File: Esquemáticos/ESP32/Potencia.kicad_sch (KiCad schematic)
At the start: 16 parts, among them U1 LM2596S-5

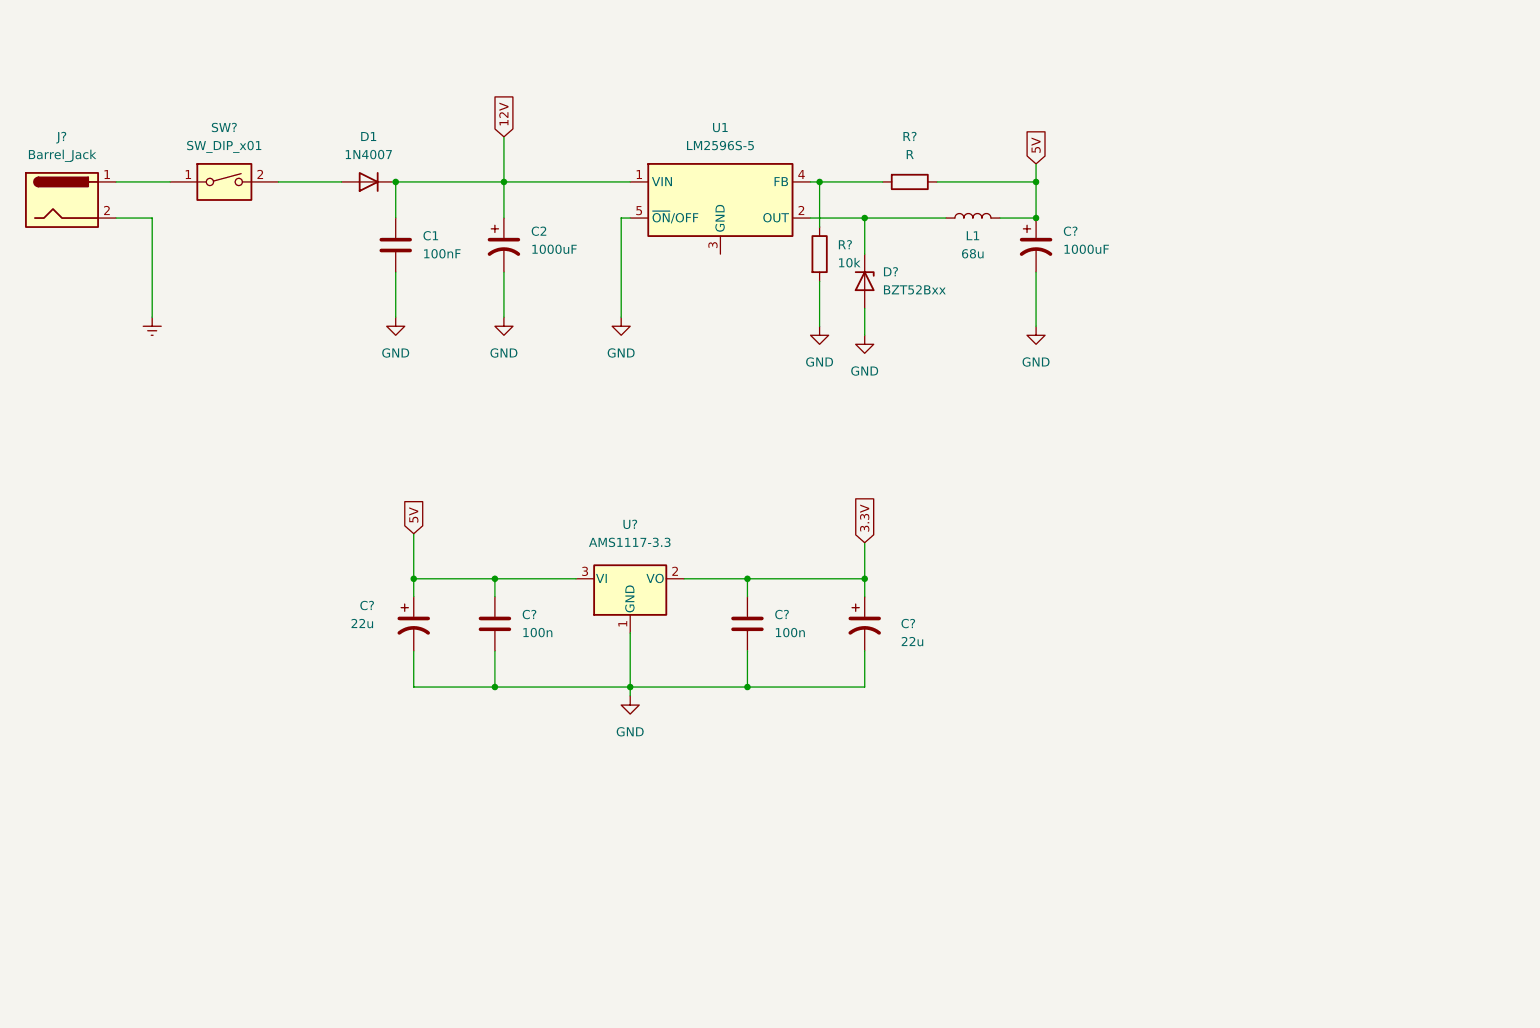
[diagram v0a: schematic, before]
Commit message: Agregada la parte de motores a la jerarquía de esquemáticos
:+1:
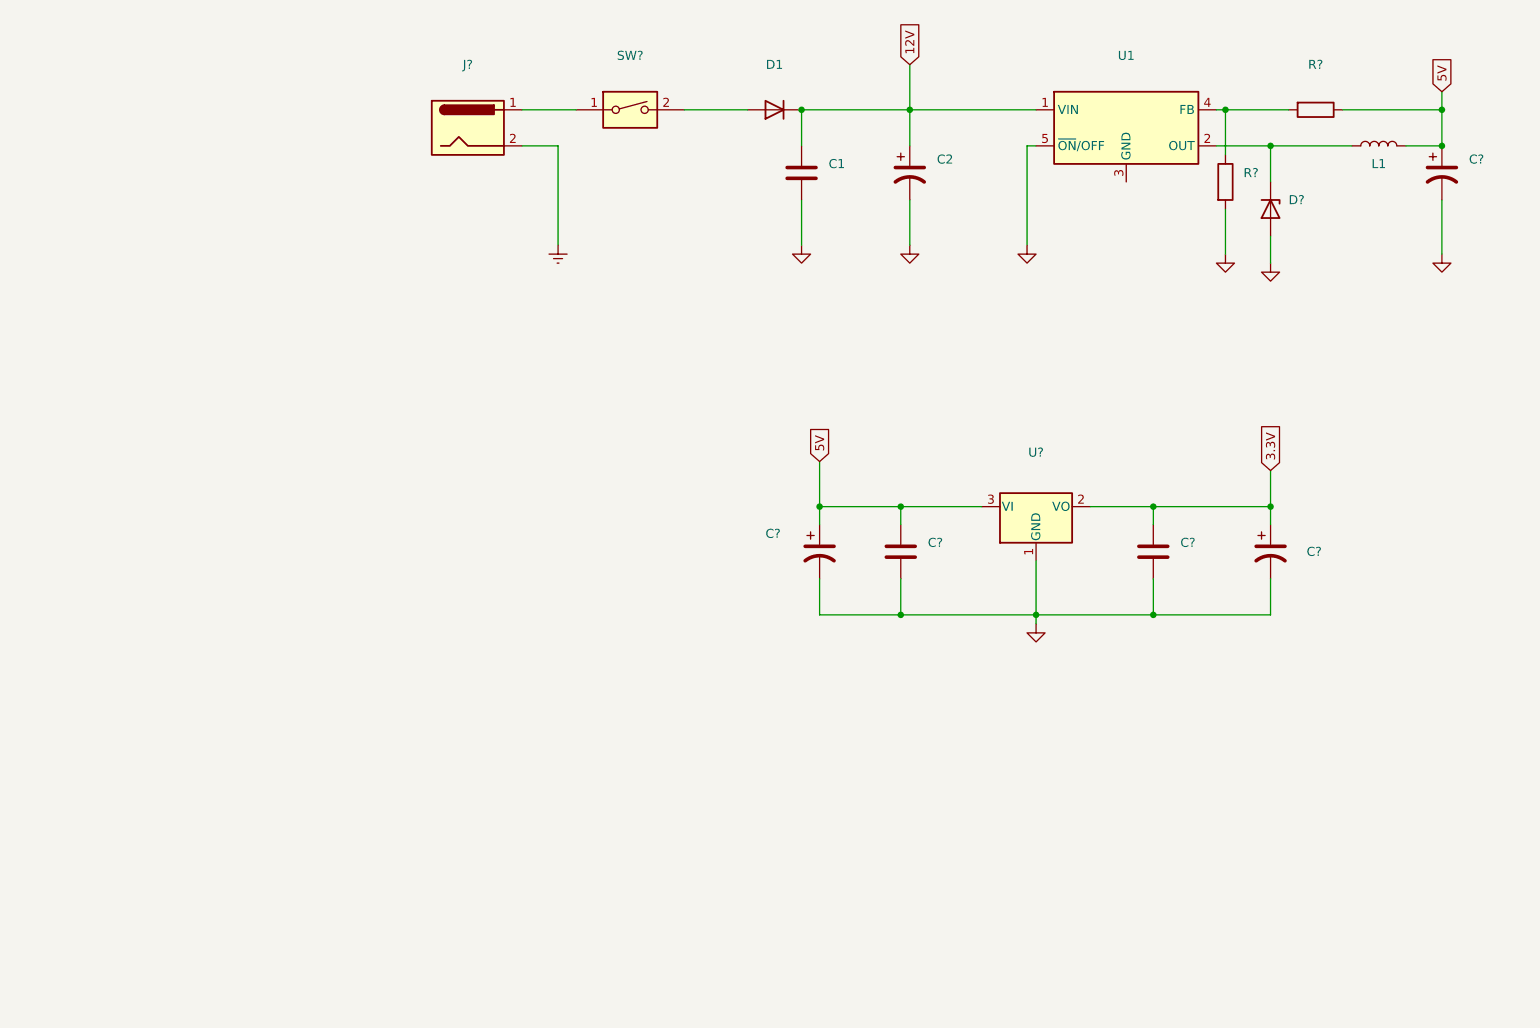
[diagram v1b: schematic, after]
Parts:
- C1: value 100nF -> (none)
- C2, C?: value 1000uF -> (none)
- C? (x2): value 100n -> (none)
- C? (x2): value 22u -> (none)
- D1: value 1N4007 -> (none); footprint Diode_THT:D_DO-41_SOD81_P10.16mm_Horizontal -> (none)
- D?: value BZT52Bxx -> (none); footprint Diode_SMD:D_SOD-123F -> (none)
- J?: value Barrel_Jack -> (none)
- L1: value 68u -> (none)
- R?: value 10k -> (none)
- R?: value R -> (none)
- SW?: value SW_DIP_x01 -> (none)
- U1: value LM2596S-5 -> (none); footprint Package_TO_SOT_SMD:TO-263-5_TabPin3 -> (none)
- U?: value AMS1117-3.3 -> (none); footprint Package_TO_SOT_SMD:SOT-223-3_TabPin2 -> (none)
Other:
- moved on the sheet: C1, C2, C?, D1, D?, J?, L1, R?, SW?, U1, U?

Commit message: Comentario sobre el zener de potencia
Comentario agregado sobre el diodo utilizado en la etapa de potencia
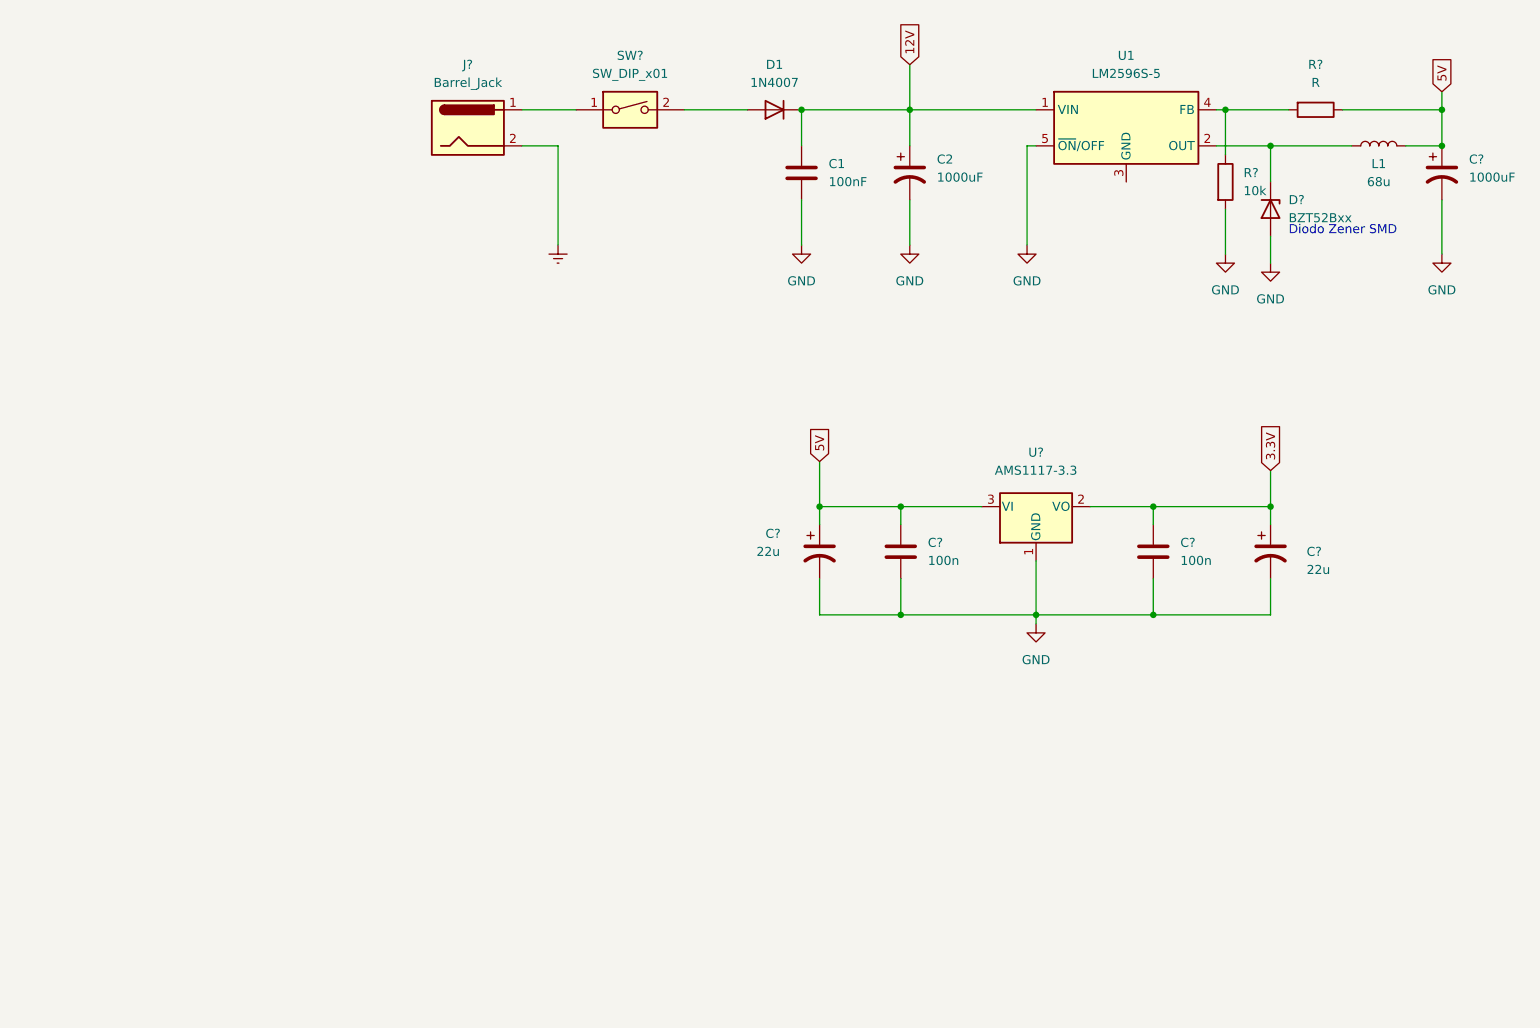
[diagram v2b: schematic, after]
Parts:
- C1: value (none) -> 100nF
- C2, C?: value (none) -> 1000uF
- C? (x2): value (none) -> 100n
- C? (x2): value (none) -> 22u
- D1: value (none) -> 1N4007; footprint (none) -> Diode_THT:D_DO-41_SOD81_P10.16mm_Horizontal
- D?: value (none) -> BZT52Bxx; footprint (none) -> Diode_SMD:D_SOD-123F
- J?: value (none) -> Barrel_Jack
- L1: value (none) -> 68u
- R?: value (none) -> 10k
- R?: value (none) -> R
- SW?: value (none) -> SW_DIP_x01
- U1: value (none) -> LM2596S-5; footprint (none) -> Package_TO_SOT_SMD:TO-263-5_TabPin3
- U?: value (none) -> AMS1117-3.3; footprint (none) -> Package_TO_SOT_SMD:SOT-223-3_TabPin2
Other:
- note added: "Diodo Zener SMD"
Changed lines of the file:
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@@
     (stroke (width 0) (type default) (color 0 0 0 0))
+  )
+  (text "Diodo Zener SMD" (at 195.58 81.28 0)
+    (effects (font (size 1.27 1.27)) (justify left bottom))
   )
   (global_label "12V" (shape input) (at 142.24 57.15 90) (fields_autoplaced)
@@
       (effects (font (size 1.27 1.27)) (justify left))
     )
-    (property "Value" "" (id 1) (at 144.78 126.9999 0)
+    (property "Value" "100n" (id 1) (at 144.78 126.9999 0)
       (effects (font (size 1.27 1.27)) (justify left))
     )
@@
       (effects (font (size 1.27 1.27)) (justify left))
     )
-    (property "Value" "" (id 1) (at 189.23 74.9299 0)
+    (property "Value" "10k" (id 1) (at 189.23 74.9299 0)
       (effects (font (size 1.27 1.27)) (justify left))
     )
@@
       (effects (font (size 1.27 1.27)) (justify left))
     )
-    (property "Value" "" (id 1) (at 195.58 78.7399 90)
-      (effects (font (size 1.27 1.27)) (justify left))
-    )
-    (property "Footprint" "" (id 2) (at 188.595 77.47 0)
+    (property "Value" "BZT52Bxx" (id 1) (at 195.58 78.7399 90)
+      (effects (font (size 1.27 1.27)) (justify left))
+    )
+    (property "Footprint" "Diode_SMD:D_SOD-123F" (id 2) (at 188.595 77.47 0)
       (effects (font (size 1.27 1.27)) hide)
     )
@@
       (effects (font (size 1.27 1.27)) hide)
     )
-    (property "Value" "" (id 1) (at 142.24 87.63 0))
+    (property "Value" "GND" (id 1) (at 142.24 87.63 0))
     (property "Footprint" "" (id 2) (at 142.24 82.55 0)
       (effects (font (size 1.27 1.27)) hide)
@@
       (effects (font (size 1.27 1.27)) hide)
     )
-    (property "Value" "" (id 1) (at 186.69 88.9 0))
+    (property "Value" "GND" (id 1) (at 186.69 88.9 0))
     (property "Footprint" "" (id 2) (at 186.69 83.82 0)
       (effects (font (size 1.27 1.27)) hide)
@@
     (in_bom yes) (on_board yes)
     (property "Reference" "L1" (id 0) (at 208.28 71.12 90))
-    (property "Value" "" (id 1) (at 208.28 73.66 90))
+    (property "Value" "68u" (id 1) (at 208.28 73.66 90))
     (property "Footprint" "" (id 2) (at 208.28 68.58 0)
       (effects (font (size 1.27 1.27)) hide)
@@
     (in_bom yes) (on_board yes) (fields_autoplaced)
     (property "Reference" "R?" (id 0) (at 199.39 57.15 90))
-    (property "Value" "" (id 1) (at 199.39 59.69 90))
+    (property "Value" "R" (id 1) (at 199.39 59.69 90))
     (property "Footprint" "" (id 2) (at 199.39 61.722 90)
       (effects (font (size 1.27 1.27)) hide)
@@
     (in_bom yes) (on_board yes) (fields_autoplaced)
     (property "Reference" "U?" (id 0) (at 160.02 111.76 0))
-    (property "Value" "" (id 1) (at 160.02 114.3 0))
-    (property "Footprint" "" (id 2) (at 160.02 114.3 0)
+    (property "Value" "AMS1117-3.3" (id 1) (at 160.02 114.3 0))
+    (property "Footprint" "Package_TO_SOT_SMD:SOT-223-3_TabPin2" (id 2) (at 160.02 114.3 0)
       (effects (font (size 1.27 1.27)) hide)
     )
@@
       (effects (font (size 1.27 1.27)) hide)
     )
-    (property "Value" "" (id 1) (at 160.02 140.97 0))
+    (property "Value" "GND" (id 1) (at 160.02 140.97 0))
     (property "Footprint" "" (id 2) (at 160.02 135.89 0)
       (effects (font (size 1.27 1.27)) hide)
@@
       (effects (font (size 1.27 1.27)) hide)
     )
-    (property "Value" "" (id 1) (at 158.75 87.63 0))
+    (property "Value" "GND" (id 1) (at 158.75 87.63 0))
     (property "Footprint" "" (id 2) (at 158.75 82.55 0)
       (effects (font (size 1.27 1.27)) hide)
@@
       (effects (font (size 1.27 1.27)) hide)
     )
-    (property "Value" "" (id 1) (at 193.04 90.17 0))
+    (property "Value" "GND" (id 1) (at 193.04 90.17 0))
     (property "Footprint" "" (id 2) (at 193.04 85.09 0)
       (effects (font (size 1.27 1.27)) hide)
@@
       (effects (font (size 1.27 1.27)) (justify left))
     )
-    (property "Value" "" (id 1) (at 130.81 73.6599 0)
+    (property "Value" "100nF" (id 1) (at 130.81 73.6599 0)
       (effects (font (size 1.27 1.27)) (justify left))
     )
@@
     (in_bom yes) (on_board yes) (fields_autoplaced)
     (property "Reference" "SW?" (id 0) (at 102.87 55.88 0))
-    (property "Value" "" (id 1) (at 102.87 58.42 0))
+    (property "Value" "SW_DIP_x01" (id 1) (at 102.87 58.42 0))
     (property "Footprint" "" (id 2) (at 102.87 63.5 0)
       (effects (font (size 1.27 1.27)) hide)
@@
       (effects (font (size 1.27 1.27)) hide)
     )
-    (property "Value" "" (id 1) (at 127 87.63 0))
+    (property "Value" "GND" (id 1) (at 127 87.63 0))
     (property "Footprint" "" (id 2) (at 127 82.55 0)
       (effects (font (size 1.27 1.27)) hide)
@@
       (effects (font (size 1.27 1.27)) (justify left))
     )
-    (property "Value" "" (id 1) (at 180.34 126.9999 0)
+    (property "Value" "100n" (id 1) (at 180.34 126.9999 0)
       (effects (font (size 1.27 1.27)) (justify left))
     )
@@
       (effects (font (size 1.27 1.27)) hide)
     )
-    (property "Value" "" (id 1) (at 92.71 86.36 0)
+    (property "Value" "Earth" (id 1) (at 92.71 86.36 0)
       (effects (font (size 1.27 1.27)) hide)
     )
@@
       (effects (font (size 1.27 1.27)) (justify left))
     )
-    (property "Value" "" (id 1) (at 120.65 125.73 0)
+    (property "Value" "22u" (id 1) (at 120.65 125.73 0)
       (effects (font (size 1.27 1.27)) (justify left))
     )
@@
       (effects (font (size 1.27 1.27)) (justify left))
     )
-    (property "Value" "" (id 1) (at 198.12 128.27 0)
+    (property "Value" "22u" (id 1) (at 198.12 128.27 0)
       (effects (font (size 1.27 1.27)) (justify left))
     )
@@
       (effects (font (size 1.27 1.27)) (justify left))
     )
-    (property "Value" "" (id 1) (at 146.05 73.0249 0)
+    (property "Value" "1000uF" (id 1) (at 146.05 73.0249 0)
       (effects (font (size 1.27 1.27)) (justify left))
     )
@@
     (in_bom yes) (on_board yes) (fields_autoplaced)
     (property "Reference" "U1" (id 0) (at 172.72 55.88 0))
-    (property "Value" "" (id 1) (at 172.72 58.42 0))
-    (property "Footprint" "" (id 2) (at 173.99 72.39 0)
+    (property "Value" "LM2596S-5" (id 1) (at 172.72 58.42 0))
+    (property "Footprint" "Package_TO_SOT_SMD:TO-263-5_TabPin3" (id 2) (at 173.99 72.39 0)
       (effects (font (size 1.27 1.27) italic) (justify left) hide)
     )
@@
     (in_bom yes) (on_board yes) (fields_autoplaced)
     (property "Reference" "D1" (id 0) (at 123.19 57.15 0))
-    (property "Value" "" (id 1) (at 123.19 59.69 0))
-    (property "Footprint" "" (id 2) (at 123.19 59.055 0)
+    (property "Value" "1N4007" (id 1) (at 123.19 59.69 0))
+    (property "Footprint" "Diode_THT:D_DO-41_SOD81_P10.16mm_Horizontal" (id 2) (at 123.19 59.055 0)
       (effects (font (size 1.27 1.27)) hide)
     )
@@
     (in_bom yes) (on_board yes) (fields_autoplaced)
     (property "Reference" "J?" (id 0) (at 80.01 57.15 0))
-    (property "Value" "" (id 1) (at 80.01 59.69 0))
+    (property "Value" "Barrel_Jack" (id 1) (at 80.01 59.69 0))
     (property "Footprint" "" (id 2) (at 81.28 67.056 0)
       (effects (font (size 1.27 1.27)) hide)
@@
       (effects (font (size 1.27 1.27)) hide)
     )
-    (property "Value" "" (id 1) (at 217.17 88.9 0))
+    (property "Value" "GND" (id 1) (at 217.17 88.9 0))
     (property "Footprint" "" (id 2) (at 217.17 83.82 0)
       (effects (font (size 1.27 1.27)) hide)
@@
       (effects (font (size 1.27 1.27)) (justify left))
     )
-    (property "Value" "" (id 1) (at 220.98 73.0249 0)
-      (effects (font (size 1.27 1.27)) (justify left))
-    )
+    (property "Value" "1000uF" (id 1) (at 220.98 73.0249 0)
+      (effects (font (size 1.27 1.27)) (justify left))
+    )
